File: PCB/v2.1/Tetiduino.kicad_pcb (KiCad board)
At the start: 2 copper layers, 53.3 x 55.2 mm, 37 parts, among them J1 Conn_01x08_Male, J2 Conn_01x06_Male, J3 Conn_01x10_Male, J4 Conn_01x08_Male, J5 AVR-ISP-6, J6 Conn_01x06_Male, SW1 SW_Push, U1 ATmega328-P, U2 LM358, U3 AMS1117-3.3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

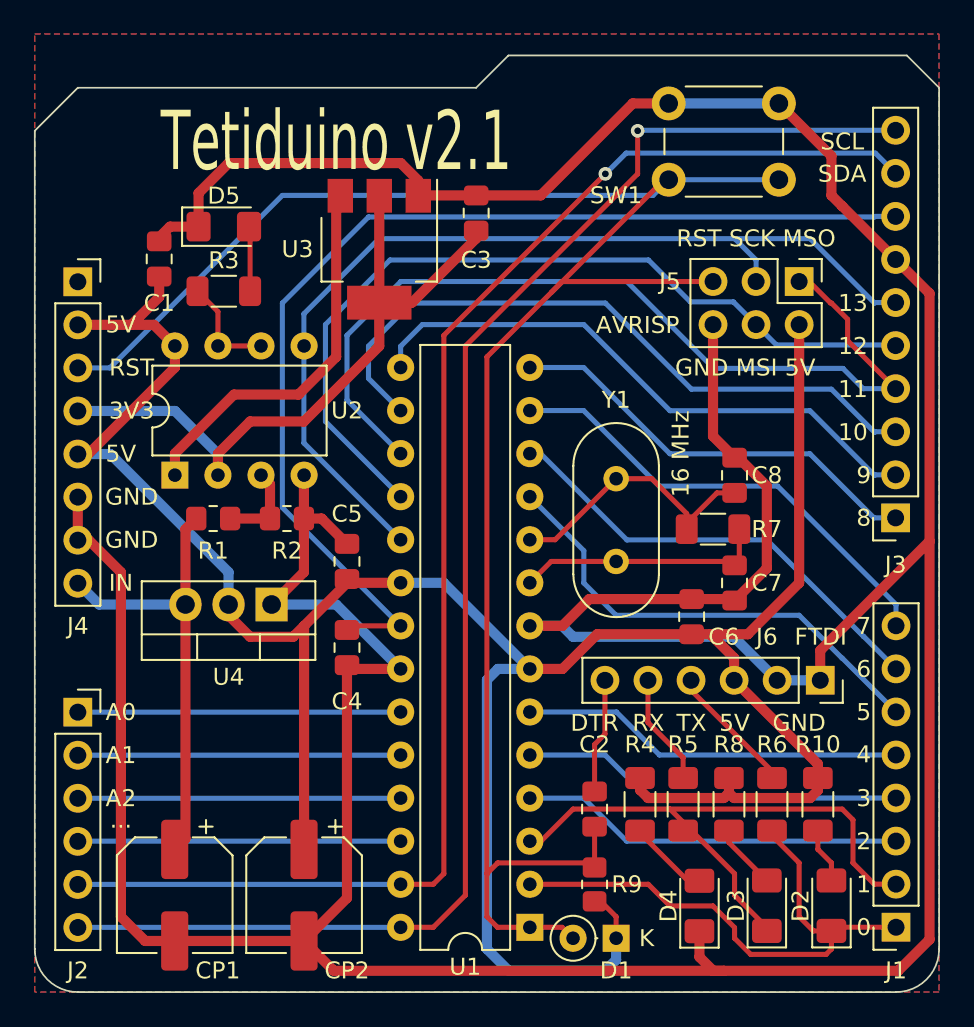
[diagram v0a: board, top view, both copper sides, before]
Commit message: Fixed PCBs for production.
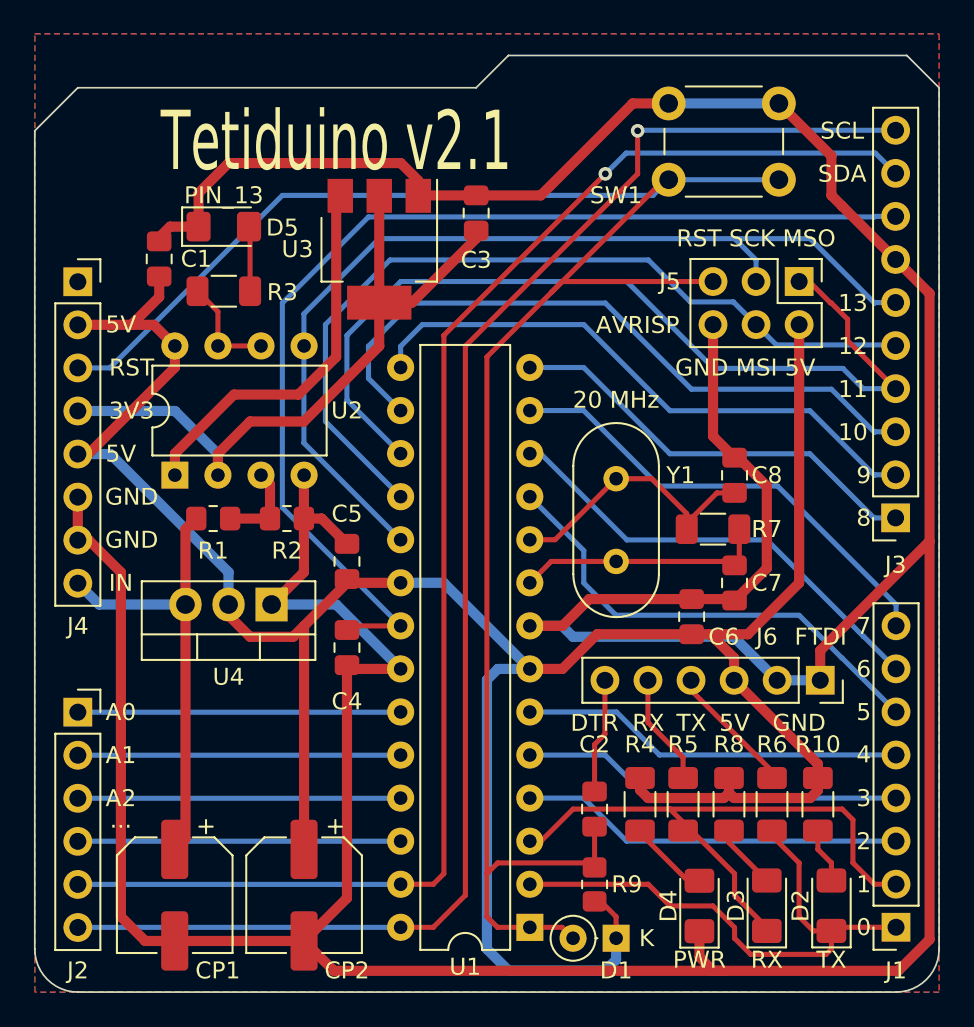
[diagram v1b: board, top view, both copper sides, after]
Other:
- board text added: "20 MHz"
- board text added: "PIN_13"
- board text added: "PWR"
- board text removed: "16 MHz"
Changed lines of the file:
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@@
       (drillshape 0)
       (scaleselection 1)
-      (outputdirectory "/home/hfrk/Projects/Tetiduino/PCB/v2.1/gerber/")
+      (outputdirectory "/home/hfrk/Projects/Tetiduino/PCB/v2.1/out/")
     )
   )
@@
     (property "Sheetname" "")
     (attr smd)
-    (fp_text reference "R3" (at 0 -1.82) (layer "F.SilkS")
+    (fp_text reference "R3" (at 3.455 0.0625) (layer "F.SilkS")
       (effects (font (size 1 1) (thickness 0.15)))
     )
@@
     (property "Sheetname" "")
     (attr smd)
-    (fp_text reference "D5" (at 0 -1.82) (layer "F.SilkS")
+    (fp_text reference "D5" (at 3.455 0.0625) (layer "F.SilkS")
       (effects (font (size 1 1) (thickness 0.15)))
     )
@@
     (property "Sheetname" "")
     (attr smd)
-    (fp_text reference "C1" (at -2.6025 0 180) (layer "F.SilkS")
+    (fp_text reference "C1" (at 0 2.185 180) (layer "F.SilkS")
       (effects (font (size 1 1) (thickness 0.15)))
     )
@@
     (property "Sheetname" "")
     (attr through_hole)
-    (fp_text reference "Y1" (at 9.525 0 180) (layer "F.SilkS")
+    (fp_text reference "Y1" (at 5.08 3.81 180) (layer "F.SilkS")
       (effects (font (size 1 1) (thickness 0.15)))
     )
@@
     (effects (font (size 1 1) (thickness 0.15)))
   )
+  (gr_text "PWR" (at 161.125 138.43) (layer "F.SilkS")
+    (effects (font (size 1 1) (thickness 0.15)))
+  )
   (gr_text "2" (at 170.815 131.445) (layer "F.SilkS")
     (effects (font (size 1 1) (thickness 0.15)))
@@
     (effects (font (size 1 1) (thickness 0.15)))
   )
-  (gr_text "SCL" (at 169.545 90.17) (layer "F.SilkS")
+  (gr_text "RX" (at 165.1 138.43) (layer "F.SilkS")
+    (effects (font (size 1 1) (thickness 0.15)))
+  )
+  (gr_text "SCL" (at 169.545 89.535) (layer "F.SilkS")
     (effects (font (size 1 1) (thickness 0.15)))
   )
@@
     (effects (font (size 1 1) (thickness 0.15)))
   )
-  (gr_text "16 MHz" (at 160.02 108.585 90) (layer "F.SilkS")
+  (gr_text "20 MHz" (at 156.21 105.41) (layer "F.SilkS")
     (effects (font (size 1 1) (thickness 0.15)))
   )
@@
     (effects (font (size 1 1) (thickness 0.15)))
   )
+  (gr_text "PIN_13" (at 133.07 93.345) (layer "F.SilkS")
+    (effects (font (size 1 1) (thickness 0.15)))
+  )
   (gr_text "3" (at 170.815 128.905) (layer "F.SilkS")
     (effects (font (size 1 1) (thickness 0.15)))
@@
     (effects (font (size 1 1) (thickness 0.15)))
   )
+  (gr_text "TX" (at 168.91 138.43) (layer "F.SilkS")
+    (effects (font (size 1 1) (thickness 0.15)))
+  )
